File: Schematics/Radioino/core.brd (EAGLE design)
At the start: 26.6 x 53.6 mm, 17 parts

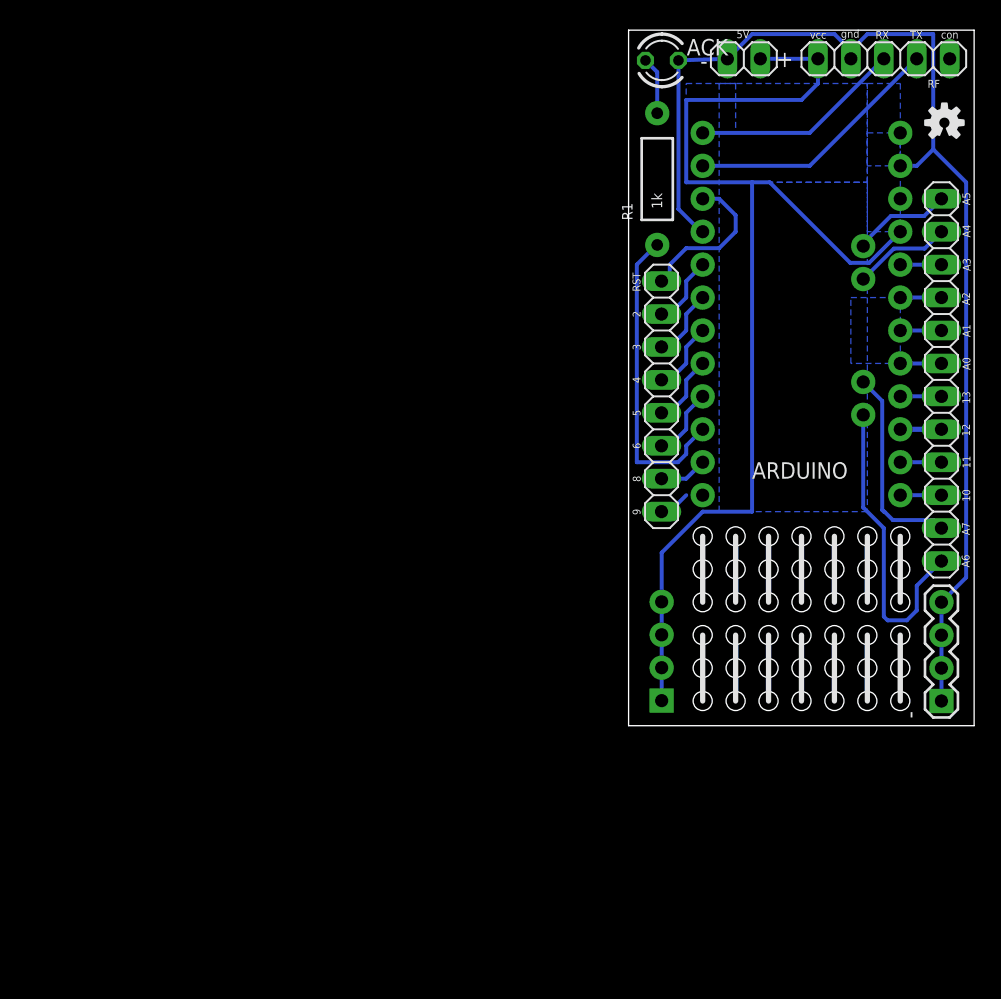
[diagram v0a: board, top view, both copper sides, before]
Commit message: New board Added the "program" button on the board
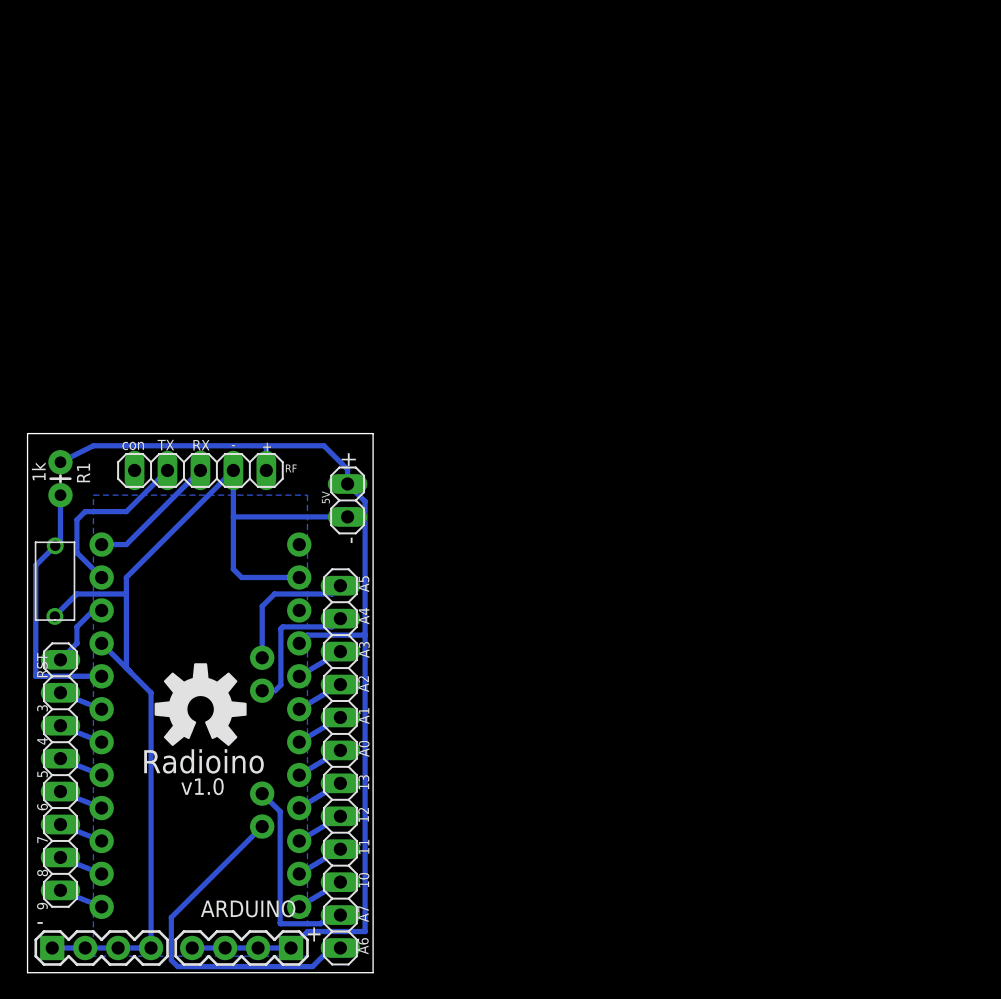
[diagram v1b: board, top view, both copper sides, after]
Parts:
- removed ACK: (no value), led:LED3MM
- removed JP1, JP2, JP3, JP4, JP5, JP6, JP7: (no value), SparkFun-Connectors:1X06_HOLES_ONLY
- added PROGRAM: PUSHBUTTON, jalf:PUSHBUTTON
- +, -: value (none) -> M04PTH; device SparkFun-Connectors:1X04 -> jalf:1X04
- R1: device SparkFun-Resistors:AXIAL-0.4 -> SparkFun-Resistors:AXIAL-0.1
- U$3: device SparkFun-Aesthetics:OSHW-LOGO-S -> SparkFun-Aesthetics:OSHW-LOGO-L
- moved U$3 73.1 mm to (13.3, 20.3)
- moved - 71.2 mm to (1.91, 1.91), turned to 0 degrees
- moved RF 61.5 mm to (13.3, 38.7)
- moved ARDUINO 56.2 mm to (13.3, 20.3)
- moved U$1 55.1 mm to (24.1, 15.9)
- moved U$2 54.8 mm to (2.54, 15.2)
- moved R1 50.9 mm to (2.54, 39.4), turned to 270 degrees
- moved 5V 45.8 mm to (24.7, 36.4), turned to 270 degrees
- moved + 34.4 mm to (20.3, 1.91), flipped to the top, turned to 180 degrees
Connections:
- removed net N$21 (its old number): ARDUINO.5, U$2.2
- removed net N$24: ACK.A, R1.P$2
- removed net N$25: JP7.1, JP7.2, JP7.3
- removed net N$26: JP2.1, JP2.2, JP2.3
- removed net N$27: JP1.1, JP1.2, JP1.3
- removed net N$28: JP6.1, JP6.2, JP6.3
- removed net N$29: JP3.1, JP3.2, JP3.3
- removed net N$30: JP4.1, JP4.2, JP4.3
- removed net N$31: JP5.1, JP5.2, JP5.3
- removed net N$32: JP7.4, JP7.5, JP7.6
- removed net N$33: JP2.4, JP2.5, JP2.6
- removed net N$34: JP1.4, JP1.5, JP1.6
- removed net N$35: JP5.4, JP5.5, JP5.6
- removed net N$36: JP4.4, JP4.5, JP4.6
- removed net N$37: JP3.4, JP3.5, JP3.6
- removed net N$38: JP6.4, JP6.5, JP6.6
- new net N$17: ARDUINO.10, U$2.7
- net 5V: now also R1.P$1
- net GND: now also PROGRAM.P$1; no longer ACK.K
- net N$23: now also ARDUINO.5, PROGRAM.P$2, R1.P$2; no longer ARDUINO.10, R1.P$1
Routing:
- net GND: track 92.5 -> 79.8 mm
- net 5V: track 88.6 -> 80.5 mm
- net N$22: track 12.4 -> 5.50 mm
- net N$13: track 16.3 -> 9.99 mm
- net N$14: track 19.9 -> 13.8 mm
- net N$21 (its old number): track 5.50 -> 0.00 mm
- net N$38: track 5.08 -> 0.00 mm
- net N$37: track 5.08 -> 0.00 mm
- net N$36: track 5.08 -> 0.00 mm
- net N$35: track 5.08 -> 0.00 mm
- net N$34: track 5.08 -> 0.00 mm
- net N$33: track 5.08 -> 0.00 mm
- net N$32: track 5.08 -> 0.00 mm
- net N$31: track 5.08 -> 0.00 mm
- net N$30: track 5.08 -> 0.00 mm
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- added copper zone on layer 16, net GND
- removed copper zone on layer 16, net N$39
- removed copper zone on layer 16, net N$40
- removed copper zone on layer 16, net N$41
- removed copper zone on layer 16, net N$42
- removed copper zone on layer 16, net N$43
- removed copper zone on layer 16, net N$44
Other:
- board size 26.6 x 53.6 mm -> 26.6 x 41.6 mm
- board text added: "Radioino"
- board text added: "v1.0"
- board text removed: "RADIOINO"
- board text removed: "v1.0 - Jalf"

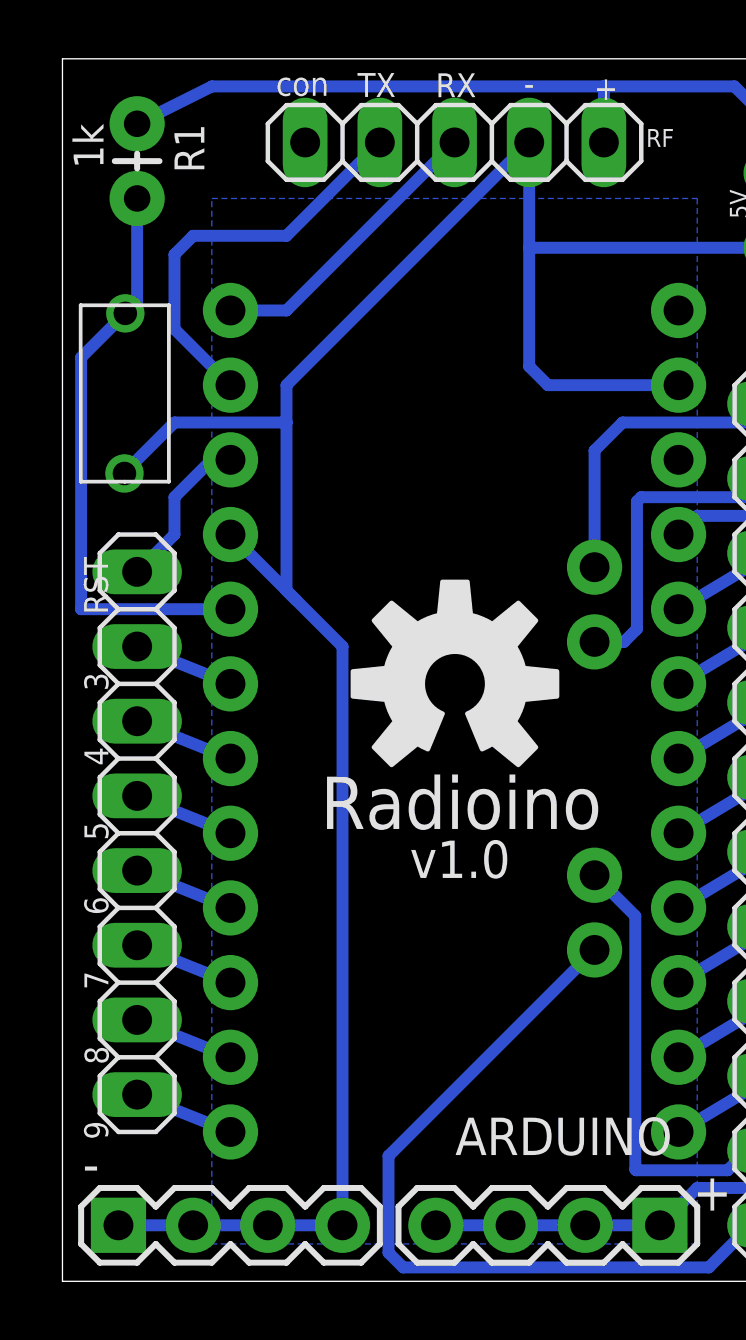
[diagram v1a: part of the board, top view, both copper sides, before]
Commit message: adjustments for the new pushbutton in the board
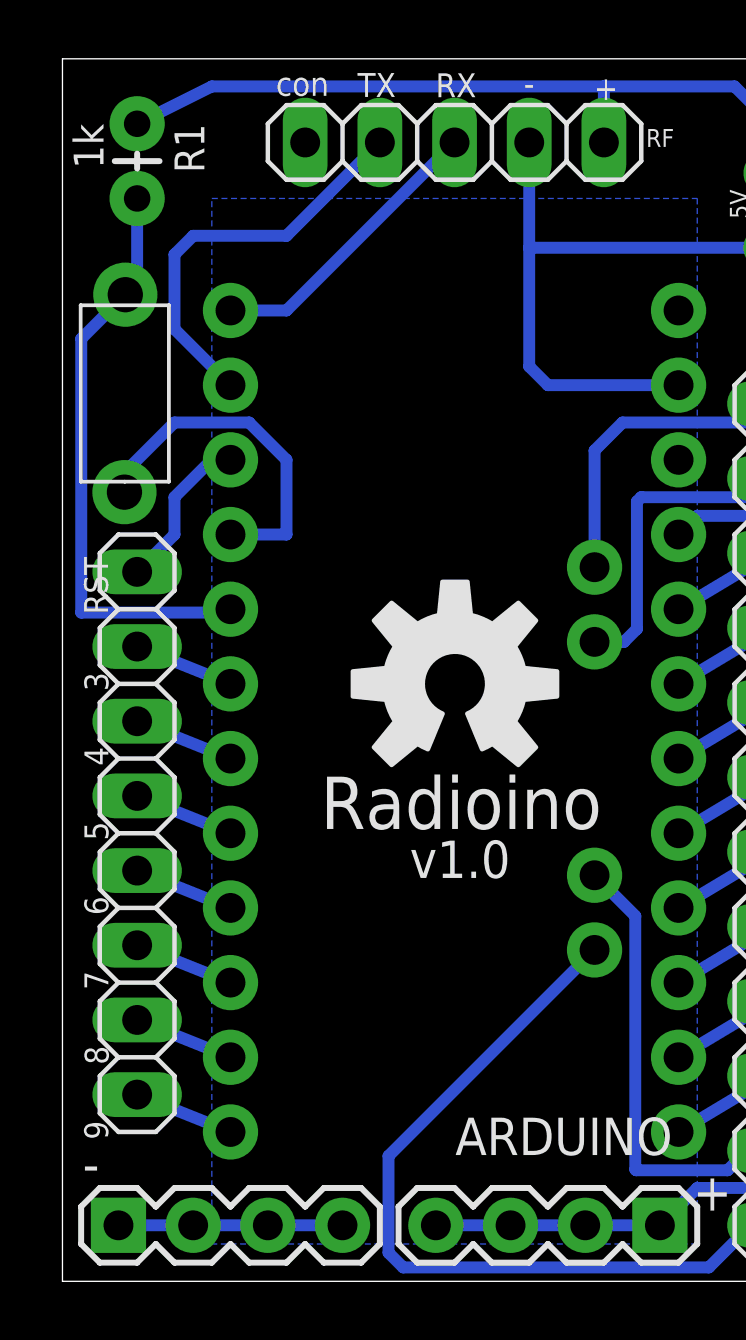
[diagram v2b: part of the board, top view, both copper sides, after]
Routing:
- net GND: track 79.8 -> 41.2 mm
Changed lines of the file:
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@@
 <wire x1="4.445" y1="1.905" x2="6.985" y2="1.905" width="0.4064" layer="16"/>
 <wire x1="6.985" y1="1.905" x2="9.525" y2="1.905" width="0.4064" layer="16"/>
-<wire x1="5.715" y1="25.4" x2="7.9375" y2="23.1775" width="0.4064" layer="16"/>
-<wire x1="7.9375" y1="23.1775" x2="9.525" y2="21.59" width="0.4064" layer="16"/>
-<wire x1="9.525" y1="21.59" x2="9.525" y2="1.905" width="0.4064" layer="16"/>
-<wire x1="2.10835" y1="27.4761" x2="2.10835" y2="27.50835" width="0.4064" layer="16"/>
-<wire x1="2.10835" y1="27.50835" x2="3.81" y2="29.21" width="0.4064" layer="16"/>
-<wire x1="3.81" y1="29.21" x2="7.62" y2="29.21" width="0.4064" layer="16"/>
-<wire x1="7.62" y1="29.21" x2="7.62" y2="23.495" width="0.4064" layer="16"/>
-<wire x1="7.62" y1="23.495" x2="7.9375" y2="23.1775" width="0.4064" layer="16"/>
-<wire x1="7.62" y1="29.21" x2="7.62" y2="30.48" width="0.4064" layer="16"/>
-<wire x1="7.62" y1="30.48" x2="15.875" y2="38.735" width="0.4064" layer="16"/>
 <wire x1="24.6838375" y1="35.152909375" x2="15.875" y2="35.152909375" width="0.4064" layer="16"/>
 <wire x1="15.875" y1="35.152909375" x2="15.875" y2="38.735" width="0.4064" layer="16"/>
@@
 <vertex x="5.08" y="1.27"/>
 </polygon>
+<wire x1="2.10835" y1="26.8411" x2="2.10835" y2="27.50835" width="0.4064" layer="16"/>
+<wire x1="2.10835" y1="27.50835" x2="3.81" y2="29.21" width="0.4064" layer="16"/>
+<wire x1="3.81" y1="29.21" x2="6.35" y2="29.21" width="0.4064" layer="16"/>
+<wire x1="6.35" y1="29.21" x2="7.62" y2="27.94" width="0.4064" layer="16"/>
+<wire x1="7.62" y1="27.94" x2="7.62" y2="25.4" width="0.4064" layer="16"/>
+<wire x1="7.62" y1="25.4" x2="5.715" y2="25.4" width="0.4064" layer="16"/>
 </signal>
 <signal name="5V">
@@
 <contactref element="ARDUINO" pad="5"/>
 <contactref element="R1" pad="P$2"/>
-<wire x1="2.137284375" y1="32.92183125" x2="2.54" y2="32.92183125" width="0.4064" layer="16"/>
-<wire x1="2.54" y1="32.92183125" x2="2.54" y2="36.83" width="0.4064" layer="16"/>
-<wire x1="2.137284375" y1="32.92183125" x2="0.635" y2="31.419546875" width="0.4064" layer="16"/>
-<wire x1="0.635" y1="31.419546875" x2="0.635" y2="22.86" width="0.4064" layer="16"/>
-<wire x1="0.635" y1="22.86" x2="5.715" y2="22.86" width="0.4064" layer="16"/>
+<wire x1="2.54" y1="36.83" x2="2.54" y2="33.959546875" width="0.4064" layer="16"/>
+<wire x1="2.54" y1="33.959546875" x2="2.137284375" y2="33.55683125" width="0.4064" layer="16"/>
+<wire x1="2.137284375" y1="33.55683125" x2="0.639253125" y2="32.0588" width="0.4064" layer="16"/>
+<wire x1="5.715" y1="22.86" x2="5.59953125" y2="22.74453125" width="0.4064" layer="16"/>
+<wire x1="5.59953125" y1="22.74453125" x2="0.639253125" y2="22.74453125" width="0.4064" layer="16"/>
+<wire x1="0.639253125" y1="22.74453125" x2="0.639253125" y2="32.0588" width="0.4064" layer="16"/>
 </signal>
 </signals>
